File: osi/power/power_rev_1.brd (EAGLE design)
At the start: 25.4 x 25.4 mm, 4 parts

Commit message: update
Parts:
- removed BAT3: (no value), SparkFun_mod:BATTCOM_20MM_PTH
- removed JP8: 8, SparkFun:1X08
- added C1, C6: (no value), SparkFun:CPOL-RADIAL-100UF-25V
- added D1: (no value), SparkFun:DIODE-1N4148
- added F1: PTCPTH, SparkFun_mod:PTC
- added IC1: (no value), SparkFun:TO-220-ALT
- added IC2: (no value), adafruit:TO92-INLINE
- added JP5: (no value), SparkFun:1X06
- added LED1: (no value), adafruit:LED3MM
- added R1: (no value), adafruit:0204V
- added U$2: (no value), DC_SYM:DC_POS_CTR
- added U$3: (no value), DC_SYM:DC_POS_CTR-BOTTOM
- JP6: value 6 -> (none); device SparkFun:1X06 -> SparkFun:1X08
- U$1: value SWITCH -> 2.1MMJACKTHM; device _my-parts:SWITCH -> adafruit:PJ-102A
- moved U$1 23.6 mm to (4.45, 18.4)
- moved JP6 23.2 mm to (5.08, 24.1)
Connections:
- removed net D8: JP6.5
- new net D10: JP5.6
- new net N$2: LED1.K, R1.2
- new net N$3: D1.A, F1.P$2
- net +3V3: now also IC2.3, JP5.4; no longer BAT3.1, JP6.4
- net +5V: now also C1.1, IC1.OUT, IC2.2, JP5.3, LED1.A; no longer JP6.3
- net AREF_D0: now also JP6.8; no longer JP8.8
- net D1: now also JP6.7; no longer JP8.7
- net D2: now also JP6.6; no longer JP8.6
- net D3: now also JP6.5; no longer JP8.5
- net D5: now also JP6.3; no longer JP8.3
- net D7: now also JP6.1; no longer JP8.1
- net D9: now also JP5.5; no longer JP6.6
- net GND: now also C1.2, C6.2, IC1.GND, IC2.1, JP5.2, R1.1, U$1.RING; no longer JP6.2, U$1.2, U$1.5
- net N$1: now also F1.P$1, U$1.TIP; no longer BAT3.2, U$1.3, U$1.6
- net SCL_D4: now also JP6.4; no longer JP8.4
- net SDA_D6: now also JP6.2; no longer JP8.2
- net V+: now also C6.1, D1.C, IC1.IN, JP5.1; no longer JP6.1
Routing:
- net V+: track 0.00 -> 59.2 mm
- net +5V: track 0.00 -> 37.8 mm
- net GND: track 22.9 -> 0.00 mm
- net N$1: track 24.7 -> 6.42 mm
- net N$3: track 0.00 -> 9.73 mm
- net N$2: track 0.00 -> 2.57 mm
- net +3V3: track 19.6 -> 18.8 mm
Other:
- board text added: "D10 D9 3V 5V GND V+"
- board text added: "Power"
- board text added: "Power Rev 1 Feb 12"
- board text added: "V+ GND 5V 3V3 D9 D10"
- board text removed: "BATT"
- board text removed: "Batt Rev 1 Feb 12"
- board text removed: "D8 D9 3V3 5V GND V+"
- board text removed: "V+ GND 5V 3V3 D8 D9"

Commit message: chuck
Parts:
- moved JP6 1.27 mm to (6.35, 24.1)
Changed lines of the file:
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@@
 <layer number="19" name="Unrouted" color="6" fill="1" visible="yes" active="yes"/>
 <layer number="20" name="Dimension" color="15" fill="1" visible="yes" active="yes"/>
-<layer number="21" name="tPlace" color="16" fill="1" visible="no" active="yes"/>
+<layer number="21" name="tPlace" color="16" fill="1" visible="yes" active="yes"/>
 <layer number="22" name="bPlace" color="14" fill="1" visible="yes" active="yes"/>
 <layer number="23" name="tOrigins" color="15" fill="1" visible="yes" active="yes"/>
@@
 <wire x1="0" y1="21.590159375" x2="0" y2="0" width="0" layer="20"/>
 <text x="0.70358125" y="2.7432" size="0.8128" layer="21" font="vector" ratio="15">V+ GND 5V 3V3 D9 D10</text>
-<text x="4.480559375" y="21.72461875" size="0.9144" layer="21" font="vector" ratio="15">D7 D6 D5 D4 D3 D2 D1 D0</text>
+<text x="5.750559375" y="21.72461875" size="0.9144" layer="21" font="vector" ratio="15">D7 D6 D5 D4 D3 D2 D1 D0</text>
 <text x="22.606" y="2.667" size="0.8128" layer="22" font="vector" ratio="15" rot="MR90">MakersBox.blogspot.com</text>
 <text x="23.749" y="2.54" size="1.27" layer="22" font="vector" ratio="15" rot="MR90">One Square Inch</text>
@@
 Rev 1
 Feb 12</text>
-<text x="23.530559375" y="21.72461875" size="0.9144" layer="22" font="vector" ratio="15" rot="MR0">D0 D1 D2 D3 D4 D5 D6 D7</text>
+<text x="24.800559375" y="21.72461875" size="0.9144" layer="22" font="vector" ratio="15" rot="MR0">D0 D1 D2 D3 D4 D5 D6 D7</text>
 <text x="14.67358125" y="2.7432" size="0.8128" layer="22" font="vector" ratio="15" rot="MR0">D10 D9 3V 5V GND V+</text>
 <text x="2.54" y="14.605" size="1.778" layer="22" font="vector" ratio="15" rot="MR90">Power</text>
@@
 <elements>
 <element name="JP5" library="SparkFun" package="1X06" value="" x="1.27" y="1.27"/>
-<element name="JP6" library="SparkFun" package="1X08" value="" x="5.08" y="24.13"/>
+<element name="JP6" library="SparkFun" package="1X08" value="" x="6.35" y="24.13"/>
 <element name="U$1" library="adafruit" package="PJ-102A" value="2.1MMJACKTHM" x="4.445" y="18.415" rot="R90"/>
 <element name="IC1" library="SparkFun" package="TO-220-ALT" value="" x="20.32" y="17.145" rot="R180"/>

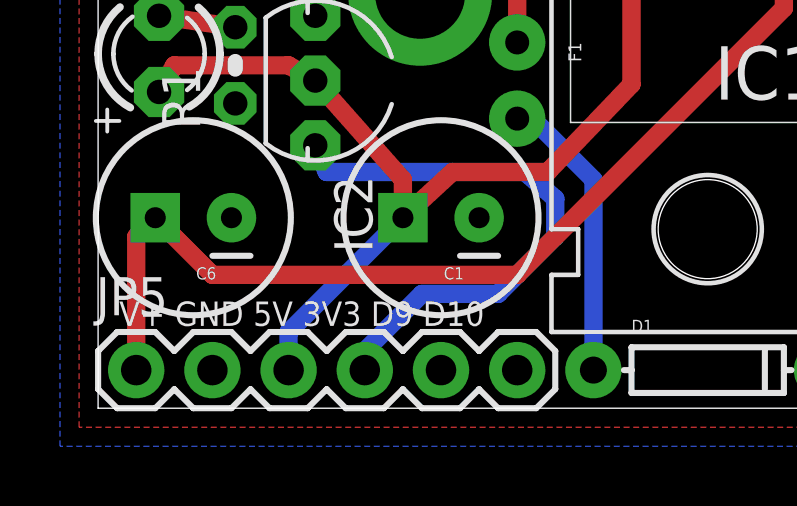
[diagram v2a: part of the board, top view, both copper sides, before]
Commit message: D9 -> D8 for INT0
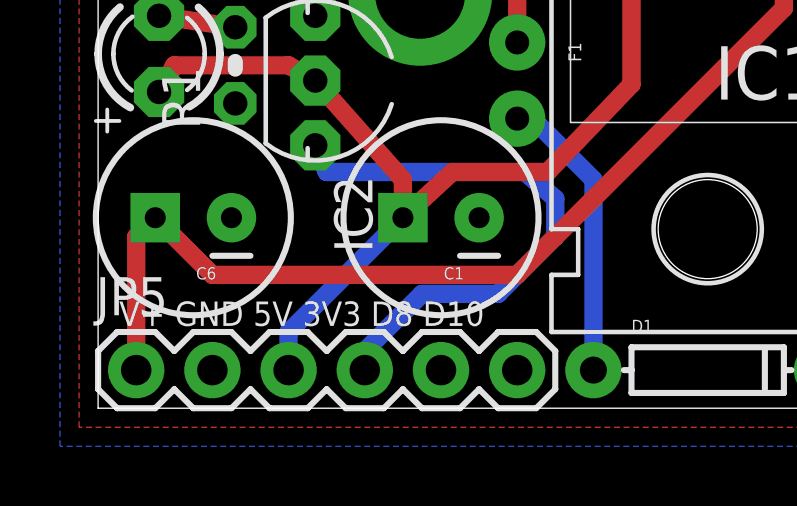
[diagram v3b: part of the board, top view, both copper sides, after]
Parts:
- C1: value (none) -> 1 uF
- C6: value (none) -> 0.33 uF
- IC1: value (none) -> UA7805CKCS
- IC2: value (none) -> MCP1702
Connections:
- net D9 renamed D8
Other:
- board text added: "D10 D8 3V 5V GND V+"
- board text added: "V+ GND 5V 3V3 D8 D10"
- board text removed: "D10 D9 3V 5V GND V+"
- board text removed: "V+ GND 5V 3V3 D9 D10"
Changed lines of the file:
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@@
 <wire x1="0.000159375" y1="21.590159375" x2="0" y2="21.590159375" width="0" layer="20"/>
 <wire x1="0" y1="21.590159375" x2="0" y2="0" width="0" layer="20"/>
-<text x="0.70358125" y="2.7432" size="0.8128" layer="21" font="vector" ratio="15">V+ GND 5V 3V3 D9 D10</text>
+<text x="0.70358125" y="2.7432" size="0.8128" layer="21" font="vector" ratio="15">V+ GND 5V 3V3 D8 D10</text>
 <text x="5.750559375" y="21.72461875" size="0.9144" layer="21" font="vector" ratio="15">D7 D6 D5 D4 D3 D2 D1 D0</text>
 <text x="22.606" y="2.667" size="0.8128" layer="22" font="vector" ratio="15" rot="MR90">MakersBox.blogspot.com</text>
@@
 Feb 12</text>
 <text x="24.800559375" y="21.72461875" size="0.9144" layer="22" font="vector" ratio="15" rot="MR0">D0 D1 D2 D3 D4 D5 D6 D7</text>
-<text x="14.67358125" y="2.7432" size="0.8128" layer="22" font="vector" ratio="15" rot="MR0">D10 D9 3V 5V GND V+</text>
+<text x="14.67358125" y="2.7432" size="0.8128" layer="22" font="vector" ratio="15" rot="MR0">D10 D8 3V 5V GND V+</text>
 <text x="2.54" y="14.605" size="1.778" layer="22" font="vector" ratio="15" rot="MR90">Power</text>
 <text x="2.286" y="21.971" size="1.778" layer="21" font="vector" ratio="15" rot="SR270">Power</text>
@@
 <element name="JP6" library="SparkFun" package="1X08" value="" x="6.35" y="24.13"/>
 <element name="U$1" library="adafruit" package="PJ-102A" value="2.1MMJACKTHM" x="4.445" y="18.415" rot="R90"/>
-<element name="IC1" library="SparkFun" package="TO-220-ALT" value="" x="20.32" y="17.145" rot="R180"/>
+<element name="IC1" library="SparkFun" package="TO-220-ALT" value="UA7805CKCS" x="20.32" y="17.145" rot="R180"/>
 <element name="D1" library="SparkFun" package="DIODE-1N4148" value="" x="20.32" y="1.27"/>
-<element name="IC2" library="adafruit" package="TO92-INLINE" value="" x="7.239" y="10.922" rot="R270"/>
-<element name="C6" library="SparkFun" package="CPOL-RADIAL-100UF-25V" value="" x="3.175" y="6.35" rot="R180"/>
-<element name="C1" library="SparkFun" package="CPOL-RADIAL-100UF-25V" value="" x="11.43" y="6.35" rot="R180"/>
+<element name="IC2" library="adafruit" package="TO92-INLINE" value="MCP1702" x="7.239" y="10.922" rot="R270"/>
+<element name="C6" library="SparkFun" package="CPOL-RADIAL-100UF-25V" value="0.33 uF" x="3.175" y="6.35" rot="R180"/>
+<element name="C1" library="SparkFun" package="CPOL-RADIAL-100UF-25V" value="1 uF" x="11.43" y="6.35" rot="R180"/>
 <element name="LED1" library="adafruit" package="LED3MM" value="" x="2.032" y="11.811" rot="R90"/>
 <element name="R1" library="adafruit" package="0204V" value="" x="4.572" y="11.43" rot="R90"/>
@@
 <wire x1="6.35" y1="2.54" x2="10.16" y2="6.35" width="0.6096" layer="16"/>
 </signal>
-<signal name="D9">
+<signal name="D8">
 <contactref element="JP5" pad="5"/>
 </signal>
